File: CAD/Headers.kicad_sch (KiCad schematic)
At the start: 62 parts, among them J1 SWD, J10 OUT_0, J11 OUT_1, J12 OUT_2, J13 TEMP_0, J14 TEMP_1, J15 TEMP_2, J16 EXPANSION, J17 ESP_DB, J19 A2543WV-5P, J2 A2543WV-2P, J20 IO_1, J21 IO_2, J22 A2543WV-2P, J23 CAN_1_OUT, J24 DRIVER_2, J25 DRIVER_1, J26 DRIVER_0, J28 SPI_DB, J3 OUT_6, J30 LASER/VFD, J31 IO_3, J33 A2543WV-4P, J34 A2543WV-4P, J35 DRIVER_3, J36 DRIVER_4, J37 DRIVER_5, J38 CAN_0_OUT, J39 PANELDUE_SD, J4 OUT_7, J41 TEMP_3, J42 DS_LED, J44 IO_7_ISO_OUT, J47 IO_8_ISO_OUT, J48 SBC, J49 A2543WV-2P, J5 OUT_8, J50 EXT_5V_IN, J51 IO_4, J53 IO_5, J54 IO_6, J55 IO_7, J56 IO_8, J59 A2543WV-2P, J6 OUT_3, J60 A2543WV-2P, J61 IO_7_ISO_IN, J62 IO_8_ISO_IN, J7 OUT_4, J8 OUT_5, J9 VIN

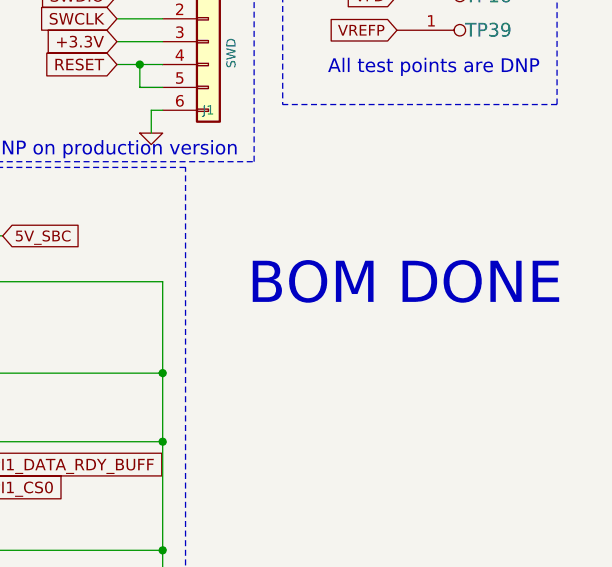
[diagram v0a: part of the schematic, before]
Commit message: WIP redoing board for new print
Removed version resistors.
Added pull-up on CMD.
Working on motors, not routed.
Added local library for custom parts.
Ran auto-cleanup of traces and vias (supervised).
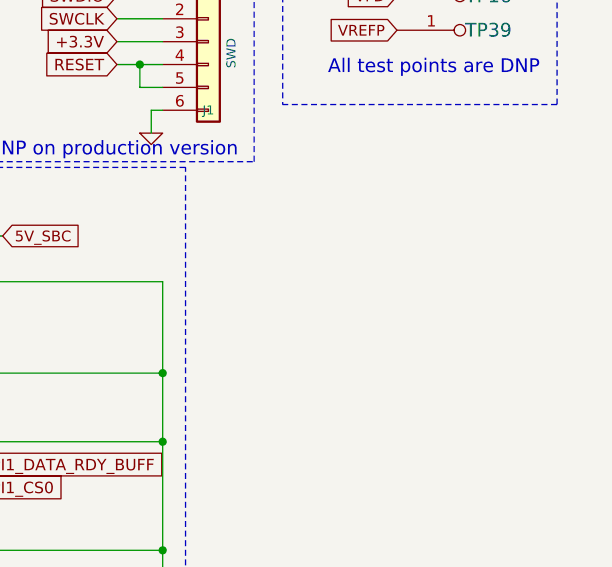
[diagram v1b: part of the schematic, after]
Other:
- note removed: "BOM DONE"
- company: Duet3d -> 3DPotter
- title: Duet 3 Main Board 6XD -> Duet 3 Main Board 3DP
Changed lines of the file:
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@@
 (kicad_sch
-	(version 20231120)
+	(version 20250114)
 	(generator "eeschema")
-	(generator_version "8.0")
+	(generator_version "9.0")
 	(paper "A3" portrait)
 	(title_block
-		(title "Duet 3 Main Board 6XD")
+		(title "Duet 3 Main Board 3DP")
 		(date "2023-02-22")
-		(rev "1.01")
-		(company "Duet3d")
-		(comment 1 "(c) Duet3D")
+		(rev "1.0")
+		(company "3DPotter")
+		(comment 1 "(c) 3DPotter")
+	)
+	(text "I/O Headers\n(not isolated)"
+		(exclude_from_sim no)
+		(at 129.54 122.555 0)
+		(effects
+			(font
+				(size 1.524 1.524)
+			)
+			(justify left bottom)
+		)
+	)
+	(text "Always on FAN for board cooling"
+		(exclude_from_sim no)
+		(at 46.355 81.026 0)
+		(effects
+			(font
+				(size 0.7112 0.7112)
+			)
+			(justify left bottom)
+		)
+	)
+	(text "External reset connection"
+		(exclude_from_sim no)
+		(at 50.8 184.15 0)
+		(effects
+			(font
+				(size 0.7112 0.7112)
+			)
+			(justify left bottom)
+		)
+	)
+	(text "I/O Headers\noptoisolated"
+		(exclude_from_sim no)
+		(at 180.975 95.25 0)
+		(effects
+			(font
+				(size 1.524 1.524)
+			)
+			(justify left bottom)
+		)
+	)
+	(text "Power, MOSFET outputs"
+		(exclude_from_sim no)
+		(at 16.51 17.78 0)
+		(effects
+			(font
+				(size 1.524 1.524)
+			)
+			(justify left bottom)
+		)
+	)
+	(text "High Current\nJST VH"
+		(exclude_from_sim no)
+		(at 64.77 55.88 0)
+		(effects
+			(font
+				(size 1.524 1.524)
+			)
+			(justify right bottom)
+		)
+	)
+	(text "additional 12V supply if\na VFD convertor is used"
+		(exclude_from_sim no)
+		(at 49.53 175.641 0)
+		(effects
+			(font
+				(size 0.7112 0.7112)
+			)
+			(justify left bottom)
+		)
+	)
+	(text "SWD"
+		(exclude_from_sim no)
+		(at 212.09 18.415 0)
+		(effects
+			(font
+				(size 1.524 1.524)
+			)
+			(justify left bottom)
+		)
+	)
+	(text "SBC Connection"
+		(exclude_from_sim no)
+		(at 182.88 43.18 0)
+		(effects
+			(font
+				(size 1.524 1.524)
+			)
+			(justify left bottom)
+		)
+	)
+	(text "All test points are DNP"
+		(exclude_from_sim no)
+		(at 274.32 29.845 0)
+		(effects
+			(font
+				(size 1.524 1.524)
+			)
+			(justify right bottom)
+		)
+	)
+	(text "DNP on production version"
+		(exclude_from_sim no)
+		(at 226.822 38.1 0)
+		(effects
+			(font
+				(size 1.524 1.524)
+			)
+		)
+	)
+	(text "ESP Connection"
+		(exclude_from_sim no)
+		(at 182.88 157.48 0)
+		(effects
+			(font
+				(size 1.524 1.524)
+			)
+			(justify left bottom)
+		)
+	)
+	(text "High Current\nTerminal\nHB9500-9.5"
+		(exclude_from_sim no)
+		(at 69.85 27.94 0)
+		(effects
+			(font
+				(size 1.524 1.524)
+			)
+			(justify right bottom)
+		)
+	)
+	(text "SPI DB Header"
+		(exclude_from_sim no)
+		(at 128.27 19.685 0)
+		(effects
+			(font
+				(size 1.524 1.524)
+			)
+			(justify left bottom)
+		)
+	)
+	(text "DotStar LED connection"
+		(exclude_from_sim no)
+		(at 177.8 18.415 0)
+		(effects
+			(font
+				(size 1.524 1.524)
+			)
+			(justify left bottom)
+		)
+	)
+	(text "4 Wire fan\nHeaders"
+		(exclude_from_sim no)
+		(at 60.325 91.44 0)
+		(effects
+			(font
+				(size 1.524 1.524)
+			)
+			(justify right bottom)
+		)
+	)
+	(text "Temperature (Thermistor &PT1000)"
+		(exclude_from_sim no)
+		(at 128.778 49.911 0)
+		(effects
+			(font
+				(size 1.524 1.524)
+			)
+			(justify left bottom)
+		)
+	)
+	(text "CAN1 and CAN0"
+		(exclude_from_sim no)
+		(at 79.375 17.145 0)
+		(effects
+			(font
+				(size 1.524 1.524)
+			)
+			(justify left bottom)
+		)
+	)
+	(text "PanelDue"
+		(exclude_from_sim no)
+		(at 128.27 92.075 0)
+		(effects
+			(font
+				(size 1.524 1.524)
+			)
+			(justify left bottom)
+		)
+	)
+	(text "Medium Current\nMolex KK"
+		(exclude_from_sim no)
+		(at 69.85 131.445 0)
+		(effects
+			(font
+				(size 1.524 1.524)
+			)
+			(justify right bottom)
+		)
+	)
+	(text "Test Points"
+		(exclude_from_sim no)
+		(at 251.46 17.78 0)
+		(effects
+			(font
+				(size 1.524 1.524)
+			)
+			(justify left bottom)
+		)
+	)
+	(text "Driver Connectors"
+		(exclude_from_sim no)
+		(at 79.375 68.58 0)
+		(effects
+			(font
+				(size 1.524 1.524)
+			)
+			(justify left bottom)
+		)
 	)
 	(junction
@@
 		)
 	)
-	(text "I/O Headers\n(not isolated)"
-		(exclude_from_sim no)
-		(at 129.54 122.555 0)
-		(effects
-			(font
-				(size 1.524 1.524)
-			)
-			(justify left bottom)
-		)
-	)
-	(text "Always on FAN for board cooling"
-		(exclude_from_sim no)
-		(at 46.355 81.026 0)
-		(effects
-			(font
-				(size 0.7112 0.7112)
-			)
-			(justify left bottom)
-		)
-	)
-	(text "External reset connection"
-		(exclude_from_sim no)
-		(at 50.8 184.15 0)
-		(effects
-			(font
-				(size 0.7112 0.7112)
-			)
-			(justify left bottom)
-		)
-	)
-	(text "I/O Headers\noptoisolated"
-		(exclude_from_sim no)
-		(at 180.975 95.25 0)
-		(effects
-			(font
-				(size 1.524 1.524)
-			)
-			(justify left bottom)
-		)
-	)
-	(text "Power, MOSFET outputs"
-		(exclude_from_sim no)
-		(at 16.51 17.78 0)
-		(effects
-			(font
-				(size 1.524 1.524)
-			)
-			(justify left bottom)
-		)
-	)
-	(text "High Current\nJST VH"
-		(exclude_from_sim no)
-		(at 64.77 55.88 0)
-		(effects
-			(font
-				(size 1.524 1.524)
-			)
-			(justify right bottom)
-		)
-	)
-	(text "additional 12V supply if\na VFD convertor is used"
-		(exclude_from_sim no)
-		(at 49.53 175.641 0)
-		(effects
-			(font
-				(size 0.7112 0.7112)
-			)
-			(justify left bottom)
-		)
-	)
-	(text "SWD"
-		(exclude_from_sim no)
-		(at 212.09 18.415 0)
-		(effects
-			(font
-				(size 1.524 1.524)
-			)
-			(justify left bottom)
-		)
-	)
-	(text "SBC Connection"
-		(exclude_from_sim no)
-		(at 182.88 43.18 0)
-		(effects
-			(font
-				(size 1.524 1.524)
-			)
-			(justify left bottom)
-		)
-	)
-	(text "All test points are DNP"
-		(exclude_from_sim no)
-		(at 274.32 29.845 0)
-		(effects
-			(font
-				(size 1.524 1.524)
-			)
-			(justify right bottom)
-		)
-	)
-	(text "DNP on production version"
-		(exclude_from_sim no)
-		(at 226.822 38.1 0)
-		(effects
-			(font
-				(size 1.524 1.524)
-			)
-		)
-	)
-	(text "ESP Connection"
-		(exclude_from_sim no)
-		(at 182.88 157.48 0)
-		(effects
-			(font
-				(size 1.524 1.524)
-			)
-			(justify left bottom)
-		)
-	)
-	(text "High Current\nTerminal\nHB9500-9.5"
-		(exclude_from_sim no)
-		(at 69.85 27.94 0)
-		(effects
-			(font
-				(size 1.524 1.524)
-			)
-			(justify right bottom)
-		)
-	)
-	(text "SPI DB Header"
-		(exclude_from_sim no)
-		(at 128.27 19.685 0)
-		(effects
-			(font
-				(size 1.524 1.524)
-			)
-			(justify left bottom)
-		)
-	)
-	(text "DotStar LED connection"
-		(exclude_from_sim no)
-		(at 177.8 18.415 0)
-		(effects
-			(font
-				(size 1.524 1.524)
-			)
-			(justify left bottom)
-		)
-	)
-	(text "4 Wire fan\nHeaders"
-		(exclude_from_sim no)
-		(at 60.325 91.44 0)
-		(effects
-			(font
-				(size 1.524 1.524)
-			)
-			(justify right bottom)
-		)
-	)
-	(text "Temperature (Thermistor &PT1000)"
-		(exclude_from_sim no)
-		(at 128.778 49.911 0)
-		(effects
-			(font
-				(size 1.524 1.524)
-			)
-			(justify left bottom)
-		)
-	)
-	(text "CAN1 and CAN0"
-		(exclude_from_sim no)
-		(at 79.375 17.145 0)
-		(effects
-			(font
-				(size 1.524 1.524)
-			)
-			(justify left bottom)
-		)
-	)
-	(text "BOM DONE\n"
-		(exclude_from_sim no)
-		(at 259.334 53.086 0)
-		(effects
-			(font
-				(size 4.572 4.572)
-			)
-		)
-	)
-	(text "PanelDue"
-		(exclude_from_sim no)
-		(at 128.27 92.075 0)
-		(effects
-			(font
-				(size 1.524 1.524)
-			)
-			(justify left bottom)
-		)
-	)
-	(text "Medium Current\nMolex KK"
-		(exclude_from_sim no)
-		(at 69.85 131.445 0)
-		(effects
-			(font
-				(size 1.524 1.524)
-			)
-			(justify right bottom)
-		)
-	)
-	(text "Test Points"
-		(exclude_from_sim no)
-		(at 251.46 17.78 0)
-		(effects
-			(font
-				(size 1.524 1.524)
-			)
-			(justify left bottom)
-		)
-	)
-	(text "Driver Connectors"
-		(exclude_from_sim no)
-		(at 79.375 68.58 0)
-		(effects
-			(font
-				(size 1.524 1.524)
-			)
-			(justify left bottom)
-		)
-	)

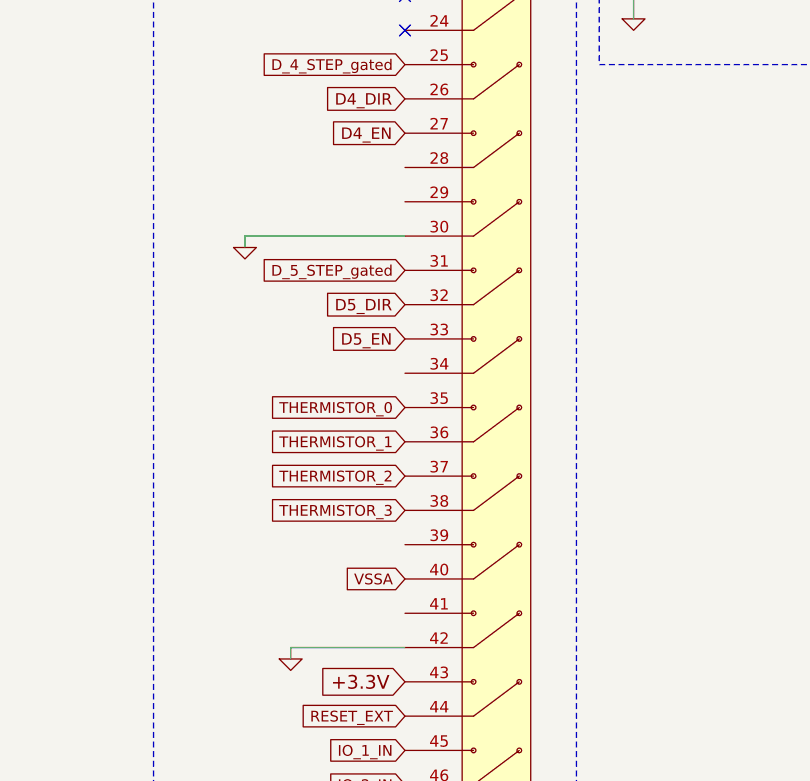
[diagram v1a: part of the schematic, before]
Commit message: motors have been routed
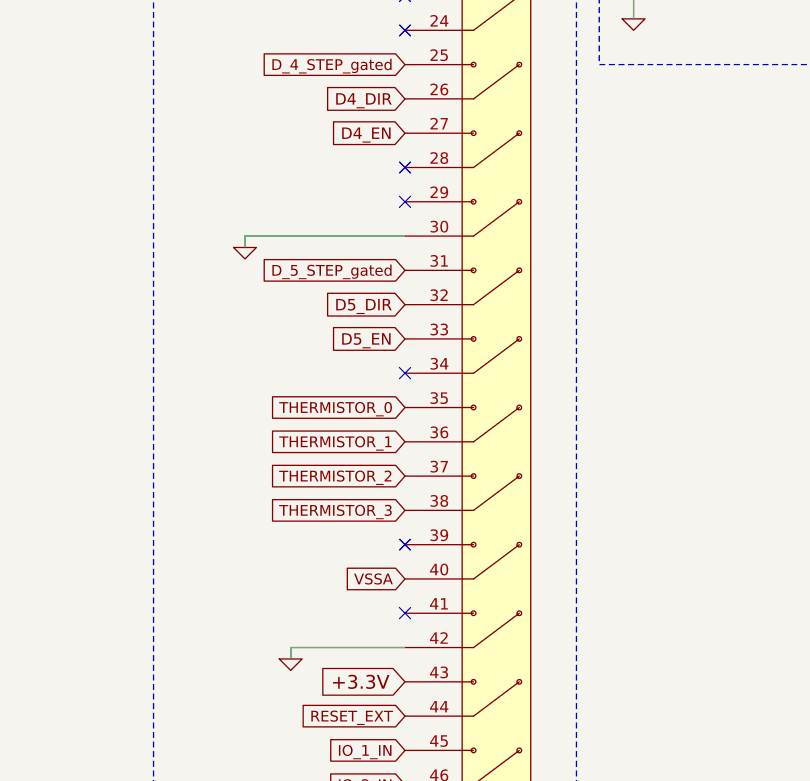
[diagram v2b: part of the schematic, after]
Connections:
- no-connect marks 23 -> 28
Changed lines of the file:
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@@
+	)
+	(no_connect
+		(at 105.41 290.83)
 	)
 	(no_connect
@@
 	(no_connect
 		(at 105.41 199.39)
+	)
+	(no_connect
+		(at 105.41 340.36)
+	)
+	(no_connect
+		(at 105.41 294.64)
 	)
 	(no_connect
@@
 	)
 	(no_connect
+		(at 105.41 332.74)
+	)
+	(no_connect
 		(at 196.215 47.625)
 	)
 	(no_connect
+		(at 105.41 313.69)
+	)
+	(no_connect

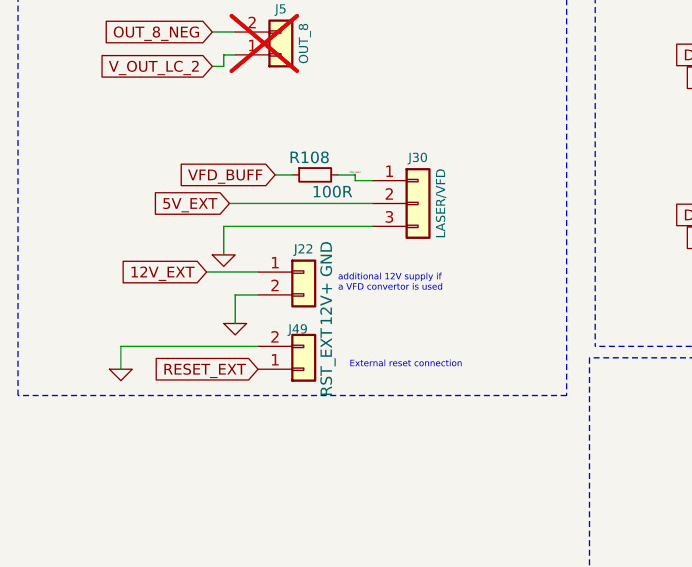
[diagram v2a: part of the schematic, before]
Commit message: Remove 12V Buck Converter
No need for it, unnecessarily complicates design, plus I dont feel like designing 2 Buck Converter layouts
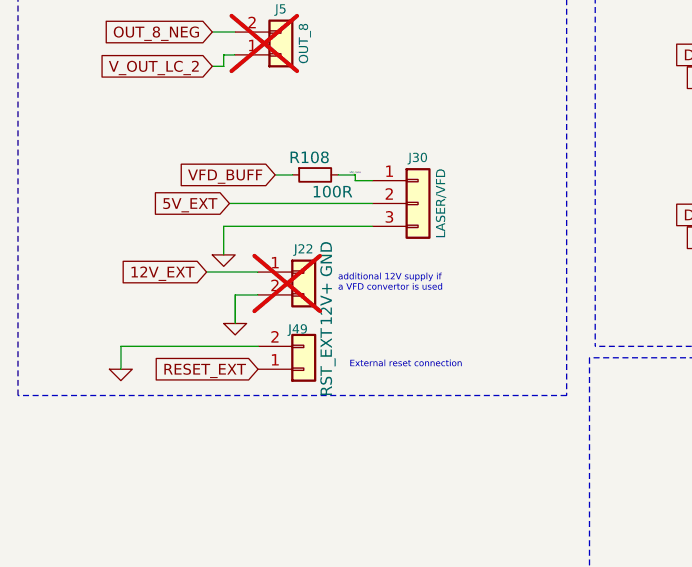
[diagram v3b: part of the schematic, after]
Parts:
- J22: now not fitted; now left out of the parts list
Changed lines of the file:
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@@
 		(unit 1)
 		(exclude_from_sim no)
-		(in_bom yes)
-		(on_board yes)
-		(dnp no)
+		(in_bom no)
+		(on_board no)
+		(dnp yes)
 		(property "Reference" "J22"
 			(at 45.72 170.815 0)

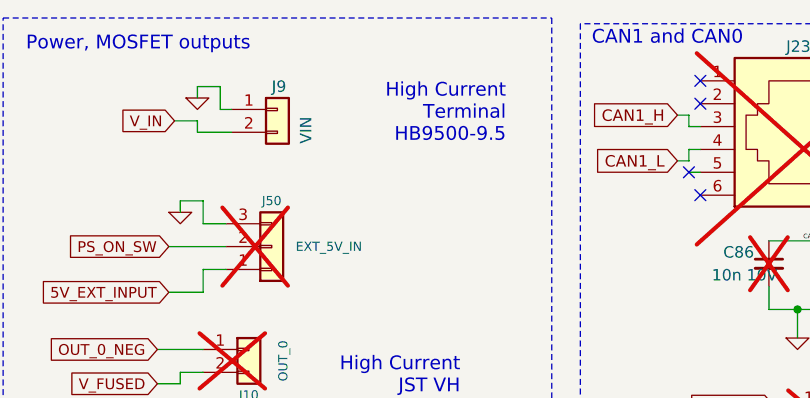
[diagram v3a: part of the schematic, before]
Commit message: New VIN Connector added
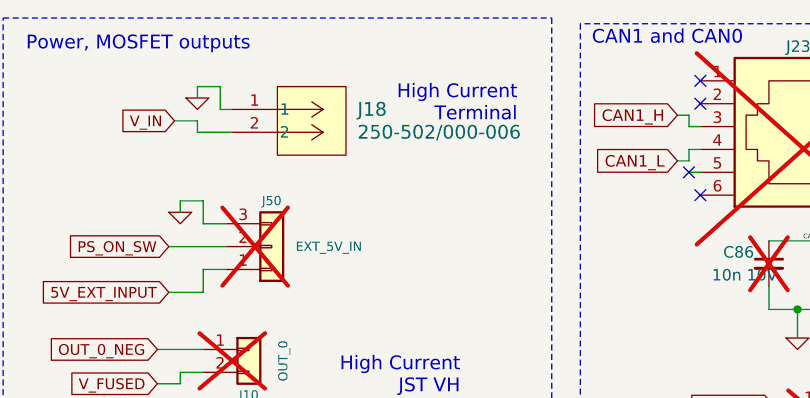
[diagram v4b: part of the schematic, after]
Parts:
- removed J9: VIN, complib:screwt-barrier-9.5mm-1x2, symbol Connector_Generic:Conn_01x02
- added J18: 250-502/000-006, CONN2_250-502/000-006_WAG, symbol 3DPotter:250-502_000-006
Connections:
- net GND: now also J18.1
- net V_IN: now also J18.2
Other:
- note added: "High Current Terminal"
- note removed: "High Current Terminal HB9500-9.5"
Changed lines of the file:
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@@
 		)
 	)
-	(text "High Current\nTerminal\nHB9500-9.5"
+	(text "High Current\nTerminal\n"
 		(exclude_from_sim no)
-		(at 69.85 27.94 0)
+		(at 71.12 25.654 0)
 		(effects
 			(font
@@
 	)
 	(symbol
-		(lib_id "Connector_Generic:Conn_01x02")
-		(at 44.45 24.13 0)
-		(unit 1)
-		(exclude_from_sim no)
-		(in_bom yes)
-		(on_board yes)
-		(dnp no)
-		(property "Reference" "J9"
-			(at 43.815 21.59 0)
-			(effects
-				(font
-					(size 1.27 1.27)
-				)
-				(justify left)
-			)
-		)
-		(property "Value" "VIN"
-			(at 47.625 27.94 90)
-			(effects
-				(font
-					(size 1.27 1.27)
-				)
-				(justify left)
-			)
-		)
-		(property "Footprint" "complib:screwt-barrier-9.5mm-1x2"
-			(at 44.45 24.13 0)
-			(effects
-				(font
-					(size 1.27 1.27)
-				)
-				(hide yes)
-			)
-		)
-		(property "Datasheet" ""
-			(at 44.45 24.13 0)
-			(effects
-				(font
-					(size 1.27 1.27)
-				)
-				(hide yes)
-			)
-		)
-		(property "Description" ""
-			(at 44.45 24.13 0)
-			(effects
-				(font
-					(size 1.27 1.27)
-				)
-				(hide yes)
-			)
-		)
-		(property "Part Number" "HB9500-9.50-2P"
-			(at 44.45 24.13 0)
-			(effects
-				(font
-					(size 1.27 1.27)
-				)
-				(hide yes)
-			)
-		)
-		(property "LCSC" "C60785"
-			(at 44.45 24.13 0)
-			(effects
-				(font
-					(size 1.524 1.524)
-				)
-				(hide yes)
-			)
-		)
-		(pin "1"
-		)
-		(pin "2"
-		)
-		(instances
-			(project ""
-				(path "/94813053-1316-4754-9fb4-4dbbf7dc780d/00000000-0000-0000-0000-000050656780"
-					(reference "J9")
-					(unit 1)
-				)
-			)
-		)
-	)
-	(symbol
 		(lib_id "Connector_Generic:Conn_02x05_Odd_Even")
 		(at 148.59 33.655 0)
@@
 					(unit 1)
 				)
+			)
+		)
+	)
+	(symbol
+		(lib_id "3DPotter:250-502_000-006")
+		(at 39.37 24.13 0)
+		(unit 1)
+		(exclude_from_sim no)
+		(in_bom yes)
+		(on_board yes)
+		(dnp no)
+		(fields_autoplaced yes)
+		(property "Reference" "J18"
+			(at 53.34 24.1299 0)
+			(effects
+				(font
+					(size 1.524 1.524)
+				)
+				(justify left)
+			)
+		)
+		(property "Value" "250-502/000-006"
+			(at 53.34 26.6699 0)
+			(effects
+				(font
+					(size 1.524 1.524)
+				)
+				(justify left)
+			)
+		)
+		(property "Footprint" "CONN2_250-502/000-006_WAG"
+			(at 48.006 30.226 0)
+			(effects
+				(font
+					(size 1.27 1.27)
+					(italic yes)
+				)
+				(hide yes)
+			)
+		)
+		(property "Datasheet" "250-502/000-006"
+			(at 48.514 34.29 0)
+			(effects
+				(font
+					(size 1.27 1.27)
+					(italic yes)
+				)
+				(hide yes)
+			)
+		)
+		(property "Description" ""
+			(at 39.37 24.13 0)
+			(effects
+				(font
+					(size 1.27 1.27)
+				)
+				(hide yes)
+			)
+		)
+		(pin "2"
+		)
+		(pin "1"
+		)
+		(instances
+			(project ""
+				(path "/94813053-1316-4754-9fb4-4dbbf7dc780d/00000000-0000-0000-0000-000050656780"
+					(reference "J18")
+					(unit 1)
+				)

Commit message: PCB Done
As far as I am aware, everything is done, still needs to be run through JLCDFM.
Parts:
- J18: footprint CONN2_250-502/000-006_WAG -> 3DPotter:CONN2_250-502&slash_000-006_WAG
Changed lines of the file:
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@@
 			)
 		)
-		(property "Footprint" "CONN2_250-502/000-006_WAG"
+		(property "Footprint" "3DPotter:CONN2_250-502&slash_000-006_WAG"
 			(at 48.006 30.226 0)
 			(effects

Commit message: QOL
Added a buttload of 3d models, 3d model of board is now usable. Also saved a lot of missing symbols and footprints, which are available in the 3DPotter Library.
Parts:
- J1: footprint complib:JST_ZH_1x06_P1.5_B6B-ZR-SM4-TF -> 3DPotter:JST_ZH_B6B-ZR_1x06_P1.50mm_Vertical
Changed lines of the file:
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@@
 			)
 		)
-		(property "Footprint" "complib:JST_ZH_1x06_P1.5_B6B-ZR-SM4-TF"
+		(property "Footprint" "3DPotter:JST_ZH_B6B-ZR_1x06_P1.50mm_Vertical"
 			(at 237.49 26.035 0)
 			(effects
